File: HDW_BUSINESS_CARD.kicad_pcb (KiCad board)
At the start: 4 copper layers, 89.4 x 51 mm, 94 parts

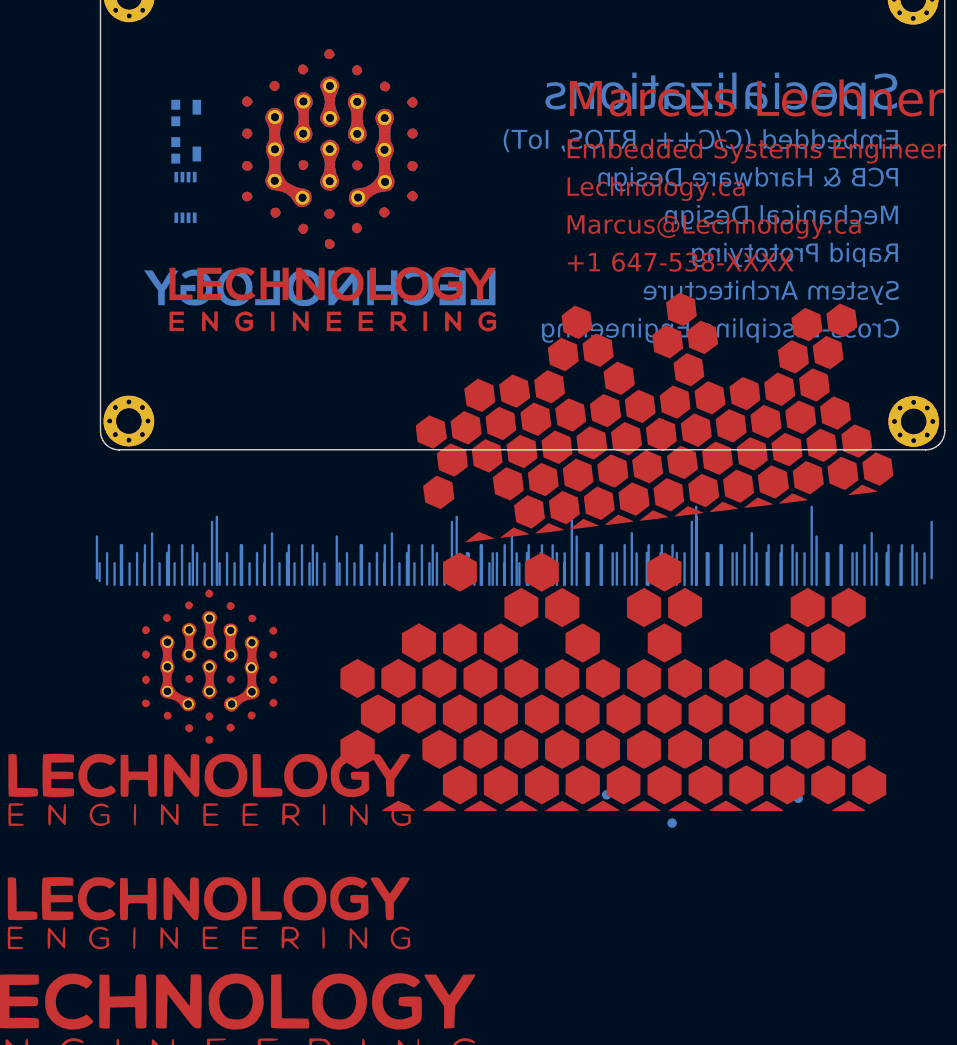
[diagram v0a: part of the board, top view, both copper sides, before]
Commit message: changed specialization text to silk screen, removed lechnology text from back, arranged logo
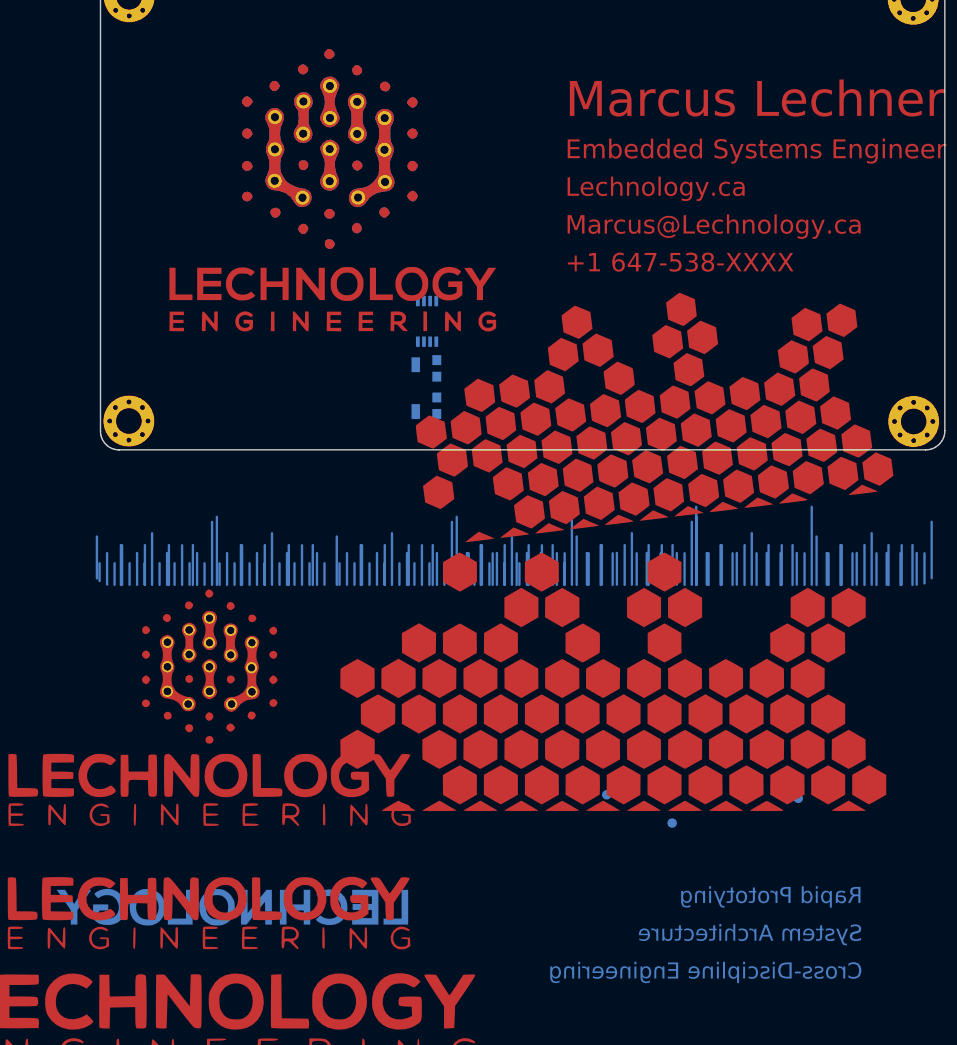
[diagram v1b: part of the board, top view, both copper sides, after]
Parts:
- added G***: LOGO, Lechnology Footprints Library:QR_Lechnology_15, B.Cu at (75.0, 91.5)
- moved G*** 66.2 mm to (64.3, 154.5)
- moved C 41.5 mm to (86.4, 97.1), turned to 90 degrees
- moved R 36.0 mm to (86.4, 93.2), turned to -90 degrees
- moved G*** 35.4 mm to (79.8, 125.0)
- moved REF** 30.3 mm to (79.6, 95.1), turned to 90 degrees
- moved REF** 28.7 mm to (85.4, 88.2), turned to 90 degrees
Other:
- board text added: "Embedded Firmware (C/C++, RTOS, IoT)"
- board text added: "PCB Design & Hardware Integration"
- board text added: "Prototyping & Mechanical Soultions"
- board text removed: "Embedded (C/C++, RTOS, IoT)"
- board text removed: "Mechanical Design"
- board text removed: "PCB & Hardware Design"

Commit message: ready for NFC coil development
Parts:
- removed (0.4mm): Texas_DSBGA-5_0.822x1.116mm_Layout2x1x2_P0.4mm, Package_BGA:Texas_DSBGA-5_0.822x1.116mm_Layout2x1x2_P0.4mm
- removed (0.5mm): Texas_DSBGA-6_0.9x1.4mm_Layout2x3_P0.5mm, Package_BGA:Texas_DSBGA-6_0.9x1.4mm_Layout2x3_P0.5mm
- removed 0.4mm: asd, Package_BGA:Texas_DSBGA-49_3.33x3.488mm_Layout7x7_P0.4mm
- removed 0201: R_0201, Resistors_SMD:R_0201
- removed 0402: R_0402, Resistors_SMD:R_0402
- removed 0603: R_0603, Resistors_SMD:R_0603
- removed 0805: R_0805, Resistors_SMD:R_0805
- removed 1206: R_1206, Resistors_SMD:R_1206
- removed 1210: R_1210, Resistors_SMD:R_1210
- removed 1806: C_1806_4516Metric_Pad1.57x1.80mm_HandSolder, Capacitor_SMD:C_1806_4516Metric_Pad1.57x1.80mm_HandSolder
- removed 1812: C_1812_4532Metric_Pad1.30x3.40mm_HandSolder, Capacitor_SMD:C_1812_4532Metric_Pad1.30x3.40mm_HandSolder
- removed 2010: R_2010_5025Metric_Pad1.52x2.65mm_HandSolder, Resistor_SMD:R_2010_5025Metric_Pad1.52x2.65mm_HandSolder
- removed 2220: C_2220_5650Metric_Pad1.97x5.40mm_HandSolder, Capacitor_SMD:C_2220_5650Metric_Pad1.97x5.40mm_HandSolder
- removed 2512: C_2512_6332Metric_Pad1.52x3.35mm_HandSolder, Capacitor_SMD:C_2512_6332Metric_Pad1.52x3.35mm_HandSolder
- removed 2920: Fuse_2920_7451Metric_Pad2.10x5.45mm_HandSolder, Fuse:Fuse_2920_7451Metric_Pad2.10x5.45mm_HandSolder
- removed 30mil, 40, 60: Measurement_Point_Round-SMD-Pad_Small, Measurement_Points:Measurement_Point_Round-SMD-Pad_Small
- removed 3x3mm: QFN-16-1EP_3x3mm_Pitch0.5mm, Housings_DFN_QFN:QFN-16-1EP_3x3mm_Pitch0.5mm
- removed 3x4mm: DFN-16-1EP_3x4mm_Pitch0.45mm, Housings_DFN_QFN:DFN-16-1EP_3x4mm_Pitch0.45mm
- removed 4*0402: R_Array_Convex_4x0402, Resistors_SMD:R_Array_Convex_4x0402
- removed 4x4mm: QFN-16-1EP_4x4mm_Pitch0.65mm, Housings_DFN_QFN:QFN-16-1EP_4x4mm_Pitch0.65mm
- removed 5: SC-70-5, TO_SOT_Packages_SMD:SC-70-5
- removed 5: SOT-23-5, TO_SOT_Packages_SMD:SOT-23-5
- removed 5x5mm: DFN-16-1EP_5x5mm_Pitch0.5mm, Housings_DFN_QFN:DFN-16-1EP_5x5mm_Pitch0.5mm
- removed 6: SC-70-6, TO_SOT_Packages_SMD:SC-70-6
- removed 6: SOT-23-6, TO_SOT_Packages_SMD:SOT-23-6
- removed 80: Measurement_Point_Round-SMD-Pad_Big, Measurement_Points:Measurement_Point_Round-SMD-Pad_Big
- removed ?: , 
- removed BGA-49: BGA_49, bga:BGA_49-0.8mm-7x7mm
- removed BGA-49: BGA_49, bga:BGA-49_CSBGA-49_0.65mm
- removed CAN10: TO-100-10, TO_SOT_Packages_THT:TO-100-10
- removed Crystal: Crystal_HC52-U_Vertical, Crystal:Crystal_HC52-U_Vertical
- removed DIP-8: DIP-8_W7.62mm, Housings_DIP:DIP-8_W7.62mm
- removed DSBGA: Texas_DSBGA-8_0.9x1.9mm_Layout2x4_P0.5mm, Package_BGA:Texas_DSBGA-8_0.9x1.9mm_Layout2x4_P0.5mm
- removed DSBGA: Texas_DSBGA-28_1.9x3.0mm_Layout4x7_P0.4mm, Package_BGA:Texas_DSBGA-28_1.9x3.0mm_Layout4x7_P0.4mm
- removed the G*** at (62.3, 129.5)
- removed the G*** at (76.2, 74.4) (x2)
- removed the G*** at (-13.7, 101.0)
- removed the G*** at (181.6, 117.8)
- removed the G*** at (62.8, 151.4)
- removed the G*** at (79.8, 125.0)
- removed the G*** at (64.3, 154.5)
- removed the G*** at (97.1, 118.5)
- removed the G*** at (59.8, 162.2)
- removed the G*** at (75.8, 88.2)
- removed the G*** at (43.9, 30.4)
- removed the G*** at (134.5, 20.4)
- removed the G*** at (62.2, 142.6)
- removed the G*** at (104.7, 124.9)
- removed the G*** at (100.0, 174.7)
- removed LQFP: LQFP-32_5x5mm_P0.5mm, Package_QFP:LQFP-32_5x5mm_P0.5mm
- removed MELF: D_MELF, Diode_SMD:D_MELF
- removed MicroMELF: D_MicroMELF, Diode_SMD:D_MicroMELF
- removed MiniMELF: MiniMELF_Standard, Diodes_SMD:MiniMELF_Standard
- removed QFN-32: QFN-32-1EP_4x4mm_Pitch0.4mm, Housings_DFN_QFN:QFN-32-1EP_4x4mm_Pitch0.4mm
- removed the REF** at (104.4, 138.3)
- removed the REF** at (192.9, 121.7)
- removed the REF** at (187.6, 121.7)
- removed the REF** at (184.2, 116.3)
- removed the REF** at (194.4, 116.1)
- removed the REF** at (187.4, 116.3)
- removed the REF** at (190.9, 116.1)
- removed the REF** at (124.7, 138.7)
- removed the REF** at (111.3, 141.3)
- removed the REF** at (82.3, 35.3)
- removed the REF** at (59.3, 45.3)
- removed SC-70: SC-70, TO_SOT_Packages_SMD:SC-70
- removed SMA: SMA_Standard, Diodes_SMD:SMA_Standard
- removed SMB: SMB_Standard, Diodes_SMD:SMB_Standard
- removed SMC: D_SMC, Diode_SMD:D_SMC
- removed SOIC-16N: SOIC-16_3.9x9.9mm_Pitch1.27mm, Housings_SOIC:SOIC-16_3.9x9.9mm_Pitch1.27mm
- removed SOIC-16W: SOIC-16W_7.5x10.3mm_Pitch1.27mm, Housings_SOIC:SOIC-16W_7.5x10.3mm_Pitch1.27mm
- removed SOT-223: SOT-223, TO_SOT_Packages_SMD:SOT-223
- removed SOT-223-5: SOT-223-5, TO_SOT_Packages_SMD:SOT-223-5
- removed SOT-223-6: SOT-223-6, TO_SOT_Packages_SMD:SOT-223-6
- removed SOT-23: SOT-23, TO_SOT_Packages_SMD:SOT-23
- removed TO-252: TO-252-2, Package_TO_SOT_SMD:TO-252-2
- removed TQFP-32: TQFP-32_7x7mm_Pitch0.8mm, Housings_QFP:TQFP-32_7x7mm_Pitch0.8mm
- removed TSSOP-16: TSSOP-16-1EP_4.4x5mm_Pitch0.65mm, Housings_SSOP:TSSOP-16-1EP_4.4x5mm_Pitch0.65mm
- removed sc-70: SC-70-8, Package_TO_SOT_SMD:SC-70-8
- removed sot-223: SOT-223-8, Package_TO_SOT_SMD:SOT-223-8
- removed sot-23: TSOT-23-8, Package_TO_SOT_SMD:TSOT-23-8
- added G***: LOGO, Lechnology Footprints Library:Lechnology_Logo_60_FLIPPED, F.Cu at (74.8, 74.1)
- added G***: LOGO, Lechnology Footprints Library:Lechnology_Text_60, F.Cu at (74.8, 76.2)
- added G***: LOGO, Lechnology Footprints Library:Lechnology_Logo_60, F.Cu at (74.8, 74.1)
- moved C 3.49 mm to (89.9, 97.0)
- moved R 3.49 mm to (89.9, 93.0)
- moved REF** 3.49 mm to (83.1, 94.9)
- moved REF** 3.49 mm to (88.9, 88.1)
- moved REF** 0.25 mm to (54.0, 54.0)
- moved REF** 0.25 mm to (54.0, 98.6)
- moved REF** 0.22 mm to (137.0, 98.6)
- moved REF** 0.17 mm to (137.0, 54.0)
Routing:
- net (no net): track 1179.2 -> 86.9 mm, vias 3 -> 0
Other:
- board text added: "Prototyping & Mechanical Solutions"
- board text removed: ".5mm"
- board text removed: "0.3mm"
- board text removed: "0.4mm"
- board text removed: "0.5mm"
- board text removed: "0.635"
- board text removed: "0.65"
- board text removed: "0.65mm"
- board text removed: "0.8mm"
- board text removed: "1"
- board text removed: "1.0mm"
- board text removed: "1/10in"
- board text removed: "10"
- board text removed: "100"
- board text removed: "12"
- board text removed: "15"
- board text removed: "2"
- board text removed: "20"
- board text removed: "3"
- board text removed: "30"
- board text removed: "4"
- board text removed: "40"
- board text removed: "5"
- board text removed: "50"
- board text removed: "6"
- board text removed: "60"
- board text removed: "7"
- board text removed: "70"
- board text removed: "75"
- board text removed: "8"
- board text removed: "80"
- board text removed: "90"
- board text removed: "BGA-49"
- board text removed: "Board Shop #"
- board text removed: "DFN-16"
- board text removed: "DIODES"
- board text removed: "IC PACKAGES"
- board text removed: "PASSIVES(imp)"
- board text removed: "PIN PITCH"
- board text removed: "Prototyping & Mechanical Soultions"
- board text removed: "QFN-16"
- board text removed: "Rpack"
- board text removed: "TRACE WIDTH(mil)"
- board text removed: "cm"
- board text removed: "mil"

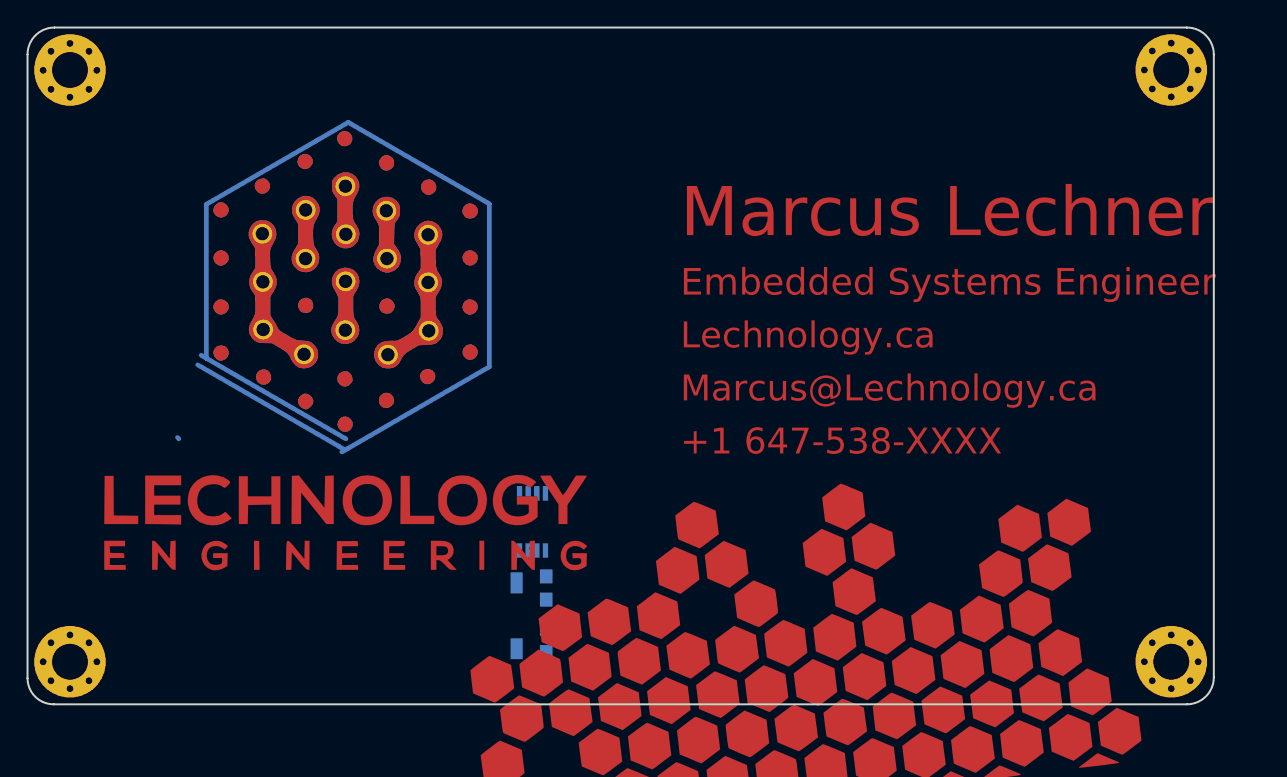
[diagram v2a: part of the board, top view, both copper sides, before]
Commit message: submitted to PCBWay, still need to update BOM with proper components and PCB coil
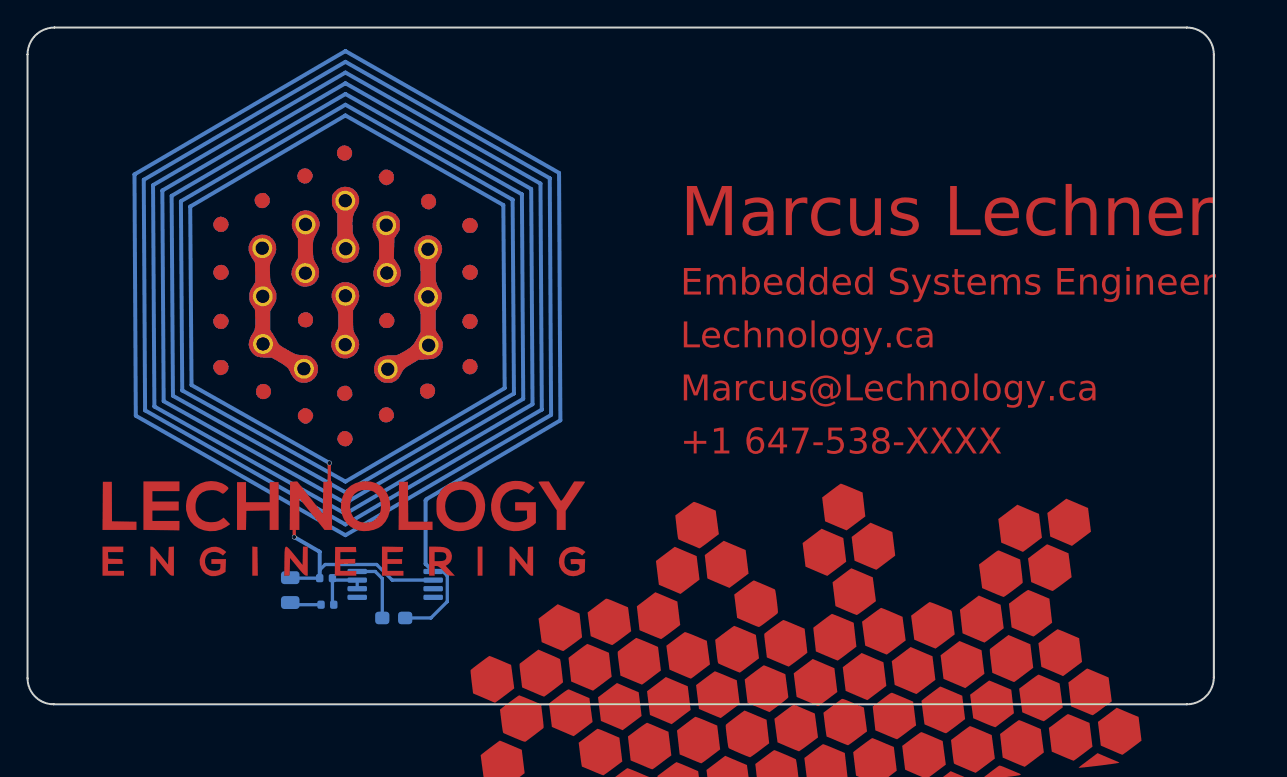
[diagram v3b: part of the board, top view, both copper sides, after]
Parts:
- removed C: C_0603_1608Metric_Pad1.05x0.95mm_HandSolder, Capacitor_SMD:C_0603_1608Metric_Pad1.05x0.95mm_HandSolder
- removed R: R_0603_1608Metric_Pad1.05x0.95mm_HandSolder, Resistor_SMD:R_0603_1608Metric_Pad1.05x0.95mm_HandSolder
- removed REF**: OSHW-Symbol_6.7x6mm_Copper, Symbol:OSHW-Symbol_6.7x6mm_Copper
- removed REF** (x4): MountingHole_2.7mm_M2.5_Pad_Via, MountingHole:MountingHole_2.7mm_M2.5_Pad_Via
- removed REF**: Back Side LED, bga:Back Side LED
- removed REF**: TSSOP-8_3x3mm_P0.65mm, Package_SO:TSSOP-8_3x3mm_P0.65mm
- added C1: 440nF, Capacitor_SMD:C_0402_1005Metric, B.Cu at (73.3, 92.3)
- added C2: 440nF, Capacitor_SMD:C_0603_1608Metric_Pad1.08x0.95mm_HandSolder, B.Cu at (78.4, 95.3)
- added D1: LED, Diode_SMD:D_0805_2012Metric, B.Cu at (70.6, 93.2)
- added R1: 47ohm, Capacitor_SMD:C_0402_1005Metric, B.Cu at (73.4, 94.3)
- added U1: NT3H1101, Package_SO:TSSOP-8_4.4x3mm_P0.65mm, B.Cu at (78.5, 92.8)
- moved G*** 19.5 mm to (94.5, 91.7)
- moved G*** 1.09 mm to (74.8, 75.2) (x2)
- moved G*** 0.46 mm to (74.6, 76.6)
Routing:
- net (no net): track 86.9 -> 0.00 mm
- net Net-(D1-K): track 0.00 -> 15.5 mm, vias 0 -> 2
- net Net-(U1-LA): track 0.00 -> 14.1 mm
- net Net-(U1-LB): track 0.00 -> 5.08 mm
- net Net-(U1-VCC): track 0.00 -> 4.62 mm
- net Net-(D1-A): track 0.00 -> 2.39 mm
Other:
- copper layers 4 -> 2
- board text removed: "--- This is a V-Scoring line"
- board text removed: "<-- This is a V-Scoring line"
- board text removed: "<-- This side routed"
- board text removed: "Rapid Prototying"
- board text removed: "This is a V-Scoring line ---"
- board text removed: "This side routed -->"

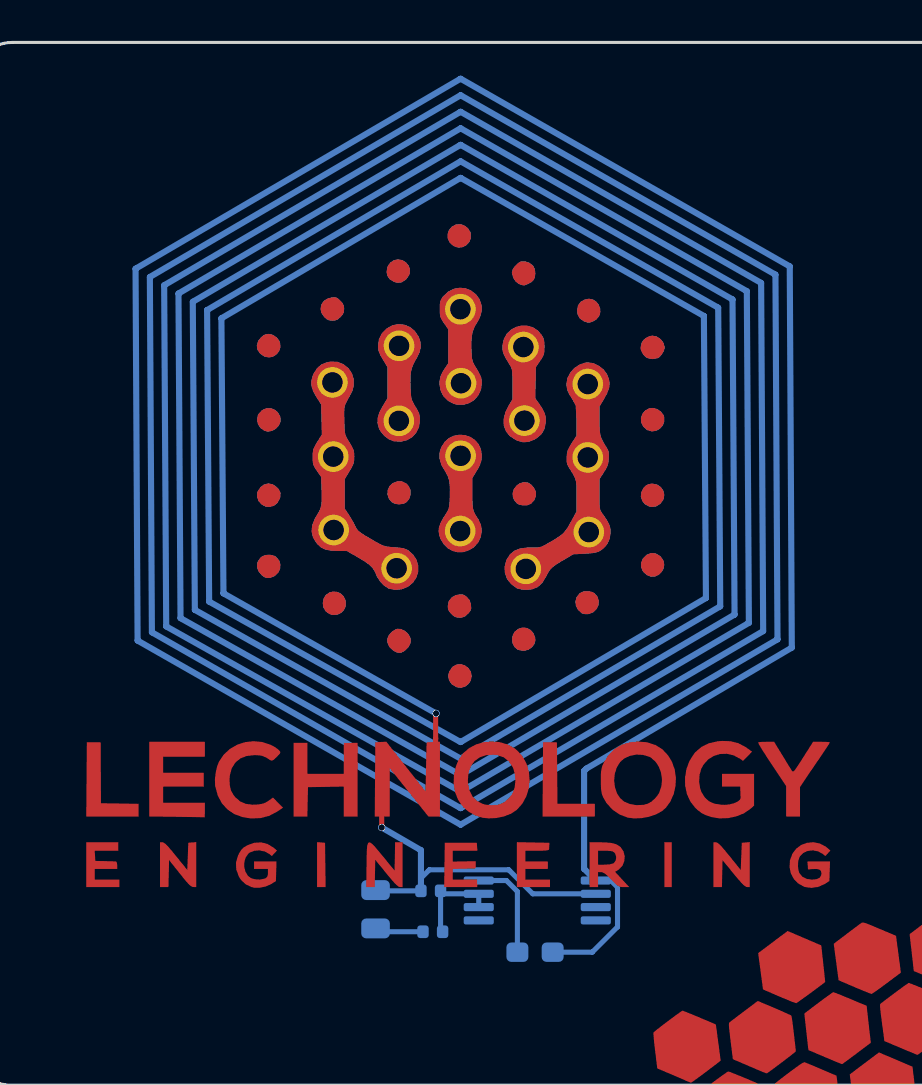
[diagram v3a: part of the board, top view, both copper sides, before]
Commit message: setup hex coil nets
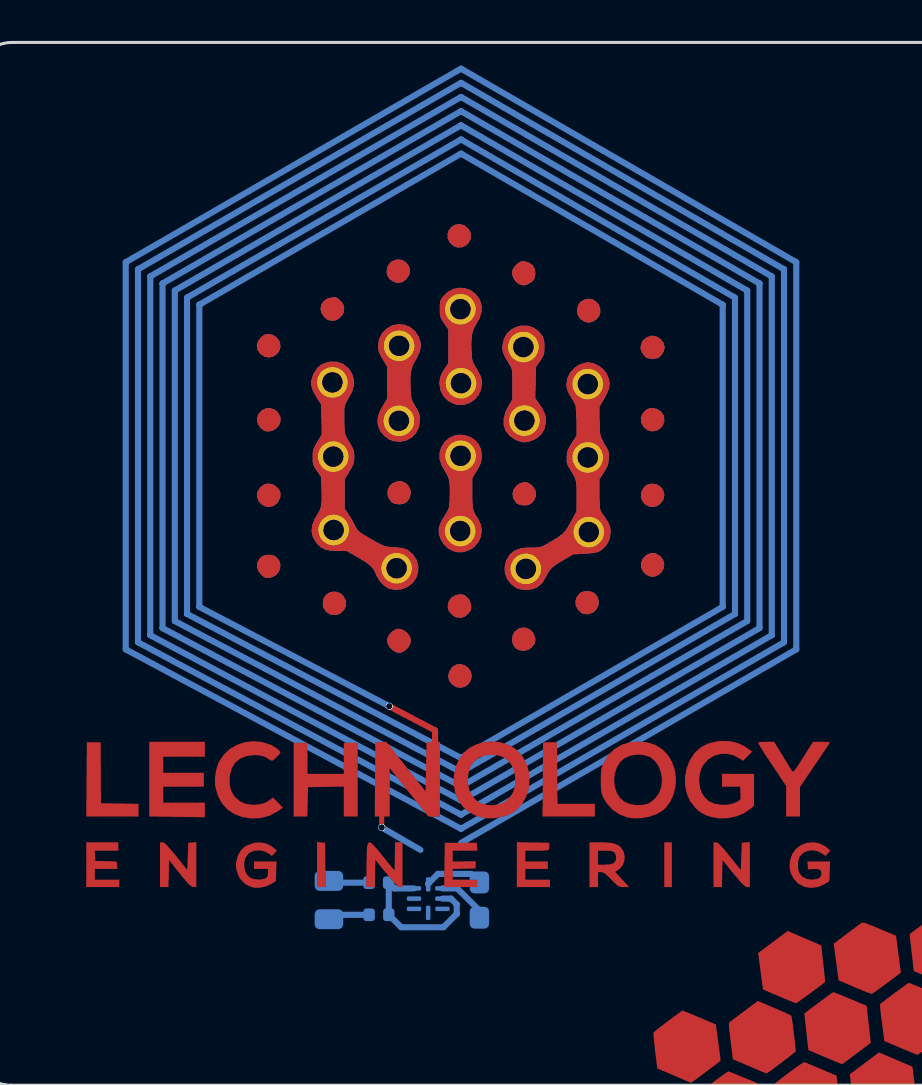
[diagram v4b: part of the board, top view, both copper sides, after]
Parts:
- C1: value 440nF -> 220nF
- U1: footprint Package_SO:TSSOP-8_4.4x3mm_P0.65mm -> Lechnology Footprints Library:QFN8P50_160X160X50L40X20N
- moved U1 5.34 mm to (73.2, 92.7)
- moved C2 3.73 mm to (75.7, 92.8), turned to -90 degrees
- moved R1 2.76 mm to (70.8, 93.5)
- moved C1 2.57 mm to (70.8, 91.9)
- moved D1 2.32 mm to (68.3, 92.8)
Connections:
- C1 pad 1: Net-(U1-VCC) -> Net-(U1-VOUT)
- R1 pad 1: Net-(U1-VCC) -> Net-(U1-VOUT)
- U1 pad 2: Net-(D1-K) -> Net-(U1-VOUT)
- U1 pad 6: Net-(U1-VCC) -> Net-(D1-K)
- U1 pad 7: Net-(U1-VCC) -> Net-(U1-VOUT)
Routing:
- net Net-(U1-LA): track 14.1 -> 2.61 mm, vias 0 -> 1
- net Net-(U1-VOUT): track 0.00 -> 8.06 mm
- net Net-(D1-K): track 15.5 -> 7.49 mm, vias 2 -> 1
- net Net-(U1-VCC): track 4.62 -> 0.00 mm
- net Net-(U1-LB): track 5.08 -> 2.91 mm
